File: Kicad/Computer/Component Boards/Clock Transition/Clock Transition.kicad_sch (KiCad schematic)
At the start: 14 parts, among them IC1 74LVC1G32GV,125, IC2 AP7365-33WG-7, IC3 74LVC1G02GV,125, IC4 74LVC74APW,118, IC5 74LVC08APW,112, IC7 74LVC74APW,118, J1 Conn_02x06_Counter_Clockwise

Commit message: Panelised Speed Board.
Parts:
- IC2: Garbage DiodesZetex AP7365-33WG-7, LDO Voltage Regulator, 600mA, 3.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 -> (none)
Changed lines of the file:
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@@
-			)
-		)
-		(property "Garbage" "DiodesZetex AP7365-33WG-7, LDO Voltage Regulator, 600mA, 3.3 V +/-2%, 2  6 Vin, 5-Pin SOT-25"
-			(at 130.81 186.182 0)
-			(effects
-				(font
-					(size 1.27 1.27)
-				)
-				(justify left)
-				(hide yes)
 			)
 		)

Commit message: Use VRML instead of STEPs for Graphics Board models.
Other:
- title: HCP65 W65C816 Clock Hold -> HCP65 Clock Transition
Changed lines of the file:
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@@
 	(paper "A4")
 	(title_block
-		(title "HCP65 W65C816 Clock Hold")
-		(date "2024-05-11")
-		(rev "V1")
+		(title "HCP65 Clock Transition")
+		(date "2025-01-04")
+		(rev "V0")
 	)
 	(junction

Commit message: Added Clock Transition.
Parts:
- added J2, J3: Pin_Header_01x06, SamacSys_Parts:PinHeader_1x06_P2.54mm_Vertical, symbol HCP65:Pin_Header_01x32
- IC5: Garbage NXP 74LVC08APW,112, Quad 2-Input AND Logic Gate, 1.2 3.6 V,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 -> (none)
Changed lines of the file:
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@@
-			)
-		)
-		(property "Garbage" "NXP 74LVC08APW,112, Quad 2-Input AND Logic Gate, 1.2  3.6 V, 14-Pin TSSOP"
-			(at 179.07 148.59 0)
-			(effects
-				(font
-					(size 1.27 1.27)
-				)
-				(hide yes)
 			)
 		)
@@
 			)
 		)
-		(property "Garbage" "NXP 74LVC08APW,112, Quad 2-Input AND Logic Gate, 1.2  3.6 V, 14-Pin TSSOP"
-			(at 90.17 93.98 0)
-			(effects
-				(font
-					(size 1.27 1.27)
-				)
-				(hide yes)
-			)
-		)
 		(pin "8"
 		)
@@
 	)
 	(symbol
+		(lib_id "HCP65:Pin_Header_01x32")
+		(at 53.34 135.89 0)
+		(unit 1)
+		(exclude_from_sim no)
+		(in_bom yes)
+		(on_board yes)
+		(dnp no)
+		(property "Reference" "J3"
+			(at 53.34 134.62 0)
+			(effects
+				(font
+					(size 1.27 1.27)
+				)
+			)
+		)
+		(property "Value" "Pin_Header_01x06"
+			(at 53.34 137.16 0)
+			(effects
+				(font
+					(size 1.27 1.27)
+				)
+			)
+		)
+		(property "Footprint" "SamacSys_Parts:PinHeader_1x06_P2.54mm_Vertical"
+			(at 53.34 139.7 0)
+			(effects
+				(font
+					(size 1.27 1.27)
+				)
+				(hide yes)
+			)
+		)
+		(property "Datasheet" "~"
+			(at 48.26 135.89 0)
+			(effects
+				(font
+					(size 1.27 1.27)
+				)
+				(hide yes)
+			)
+		)
+		(property "Description" ""
+			(at 53.34 135.89 0)
+			(effects
+				(font
+					(size 1.27 1.27)
+				)
+				(hide yes)
+			)
+		)
+		(instances
+			(project "Clock Transition"
+				(path "/5ce90b85-49a2-4937-86c7-662b0d6f8431"
+					(reference "J3")
+					(unit 1)
+				)
+			)
+		)
+	)
+	(symbol
 		(lib_id "Nexperia:74LVC08APW,112_Multi")
 		(at 209.55 90.17 0)
@@
 		(property "Silkscreen" "74LVC08"
 			(at 222.25 100.33 0)
-			(effects
-				(font
-					(size 1.27 1.27)
-				)
-				(hide yes)
-			)
-		)
-		(property "Garbage" "NXP 74LVC08APW,112, Quad 2-Input AND Logic Gate, 1.2  3.6 V, 14-Pin TSSOP"
-			(at 209.55 90.17 0)
 			(effects
 				(font
@@
 	)
 	(symbol
+		(lib_id "HCP65:Pin_Header_01x32")
+		(at 53.34 130.81 0)
+		(mirror y)
+		(unit 1)
+		(exclude_from_sim no)
+		(in_bom yes)
+		(on_board yes)
+		(dnp no)
+		(property "Reference" "J2"
+			(at 53.34 129.54 0)
+			(effects
+				(font
+					(size 1.27 1.27)
+				)
+			)
+		)
+		(property "Value" "Pin_Header_01x06"
+			(at 53.34 132.08 0)
+			(effects
+				(font
+					(size 1.27 1.27)
+				)
+			)
+		)
+		(property "Footprint" "SamacSys_Parts:PinHeader_1x06_P2.54mm_Vertical"
+			(at 53.34 134.62 0)
+			(effects
+				(font
+					(size 1.27 1.27)
+				)
+				(hide yes)
+			)
+		)
+		(property "Datasheet" "~"
+			(at 58.42 130.81 0)
+			(effects
+				(font
+					(size 1.27 1.27)
+				)
+				(hide yes)
+			)
+		)
+		(property "Description" ""
+			(at 53.34 130.81 0)
+			(effects
+				(font
+					(size 1.27 1.27)
+				)
+				(hide yes)
+			)
+		)
+		(instances
+			(project "Clock Transition"
+				(path "/5ce90b85-49a2-4937-86c7-662b0d6f8431"
+					(reference "J2")
+					(unit 1)
+				)
+			)
+		)
+	)
+	(symbol
 		(lib_id "HCP65:C_0805")
 		(at 107.95 175.26 0)
@@
 			(effects
 				(font
-					(size 1.27 1.27)
-				)
-				(hide yes)
-			)
-		)
-		(property "Garbage" "NXP 74LVC08APW,112, Quad 2-Input AND Logic Gate, 1.2  3.6 V, 14-Pin TSSOP"
-			(at 210.82 34.29 0)
-			(effects
-				(font

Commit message: Upgraded all Compnent Boards to Kicad 9.0.
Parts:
- renumbered C27 to C43, C27 to C44
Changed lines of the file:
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@@
 (kicad_sch
-	(version 20231120)
+	(version 20250114)
 	(generator "eeschema")
-	(generator_version "8.0")
+	(generator_version "9.0")
 	(paper "A4")
 	(title_block
@@
 	(label "GND"
 		(at 179.07 151.13 180)
-		(fields_autoplaced yes)
 		(effects
 			(font
@@
 	(label "3.3V"
 		(at 168.91 36.83 180)
-		(fields_autoplaced yes)
 		(effects
 			(font
@@
 	(label "3.3V"
 		(at 143.51 148.59 0)
-		(fields_autoplaced yes)
 		(effects
 			(font
@@
 	(label "GND"
 		(at 143.51 153.67 0)
-		(fields_autoplaced yes)
 		(effects
 			(font
@@
 	(label "3.3V"
 		(at 273.05 69.85 0)
-		(fields_autoplaced yes)
 		(effects
 			(font
@@
 	(label "Clock1_{Q}"
 		(at 194.31 36.83 0)
-		(fields_autoplaced yes)
 		(effects
 			(font
@@
 	(label "3.3V"
 		(at 115.57 92.71 0)
-		(fields_autoplaced yes)
 		(effects
 			(font
@@
 	(label "GND"
 		(at 168.91 44.45 180)
-		(fields_autoplaced yes)
 		(effects
 			(font
@@
 	(label "~{Reset}"
 		(at 129.54 97.79 180)
-		(fields_autoplaced yes)
 		(effects
 			(font
@@
 	(label "GND"
 		(at 91.44 43.18 180)
-		(fields_autoplaced yes)
 		(effects
 			(font
@@
 	(label "3.3V"
 		(at 123.19 184.15 180)
-		(fields_autoplaced yes)
 		(effects
 			(font
@@
 	(label "GND"
 		(at 113.03 175.26 0)
-		(fields_autoplaced yes)
 		(effects
 			(font
@@
 	(label "3.3V"
 		(at 123.19 175.26 180)
-		(fields_autoplaced yes)
 		(effects
 			(font
@@
 	(label "3.3V"
 		(at 92.71 175.26 180)
-		(fields_autoplaced yes)
 		(effects
 			(font
@@
 	(label "GND"
 		(at 90.17 99.06 180)
-		(fields_autoplaced yes)
 		(effects
 			(font
@@
 	(label "GND"
 		(at 210.82 39.37 180)
-		(fields_autoplaced yes)
 		(effects
 			(font
@@
 	(label "Clock"
 		(at 273.05 72.39 0)
-		(fields_autoplaced yes)
 		(effects
 			(font
@@
 	(label "3.3V"
 		(at 204.47 147.32 0)
-		(fields_autoplaced yes)
 		(effects
 			(font
@@
 	(label "GND"
 		(at 100.33 153.67 0)
-		(fields_autoplaced yes)
 		(effects
 			(font
@@
 	(label "~{Select Fast}"
 		(at 60.96 38.1 180)
-		(fields_autoplaced yes)
 		(effects
 			(font
@@
 	(label "3.3V"
 		(at 107.95 175.26 180)
-		(fields_autoplaced yes)
 		(effects
 			(font
@@
 	(label "GND"
 		(at 130.81 44.45 180)
-		(fields_autoplaced yes)
 		(effects
 			(font
@@
 	(label "GND"
 		(at 128.27 175.26 0)
-		(fields_autoplaced yes)
 		(effects
 			(font
@@
 	(label "3.3V"
 		(at 116.84 36.83 0)
-		(fields_autoplaced yes)
 		(effects
 			(font
@@
 	(label "GND"
 		(at 179.07 153.67 180)
-		(fields_autoplaced yes)
 		(effects
 			(font
@@
 	(label "3.3V"
 		(at 193.04 90.17 0)
-		(fields_autoplaced yes)
 		(effects
 			(font
@@
 	(label "3.3V"
 		(at 154.94 90.17 0)
-		(fields_autoplaced yes)
 		(effects
 			(font
@@
 	(label "Slow Clock"
 		(at 60.96 78.74 180)
-		(fields_autoplaced yes)
 		(effects
 			(font
@@
 	(label "3.3V"
 		(at 130.81 36.83 180)
-		(fields_autoplaced yes)
 		(effects
 			(font
@@
 	(label "GND"
 		(at 113.03 184.15 0)
-		(fields_autoplaced yes)
 		(effects
 			(font
@@
 	(label "Fast Clock"
 		(at 60.96 22.86 180)
-		(fields_autoplaced yes)
 		(effects
 			(font
@@
 	(label "3.3V"
 		(at 107.95 184.15 180)
-		(fields_autoplaced yes)
 		(effects
 			(font
@@
 	(label "GND"
 		(at 97.79 175.26 0)
-		(fields_autoplaced yes)
 		(effects
 			(font
@@
 	(label "GND"
 		(at 247.65 76.2 180)
-		(fields_autoplaced yes)
 		(effects
 			(font
@@
 	(label "~{Clock1}_{Q}"
 		(at 194.31 39.37 0)
-		(fields_autoplaced yes)
 		(effects
 			(font
@@
 	(label "GND"
 		(at 209.55 95.25 180)
-		(fields_autoplaced yes)
 		(effects
 			(font
@@
 	(label "GND"
 		(at 129.54 100.33 180)
-		(fields_autoplaced yes)
 		(effects
 			(font
@@
 	(label "Clock2_{Q}"
 		(at 193.04 92.71 0)
-		(fields_autoplaced yes)
 		(effects
 			(font
@@
 	(label "3.3V"
 		(at 167.64 92.71 180)
-		(fields_autoplaced yes)
 		(effects
 			(font
@@
 	(label "~{Reset}"
 		(at 130.81 41.91 180)
-		(fields_autoplaced yes)
 		(effects
 			(font
@@
 	(label "~{Reset}"
 		(at 167.64 97.79 180)
-		(fields_autoplaced yes)
 		(effects
 			(font
@@
 	(label "GND"
 		(at 167.64 100.33 180)
-		(fields_autoplaced yes)
 		(effects
 			(font
@@
 	(label "GND"
 		(at 179.07 148.59 180)
-		(fields_autoplaced yes)
 		(effects
 			(font
@@
 	(label "3.3V"
 		(at 194.31 34.29 0)
-		(fields_autoplaced yes)
 		(effects
 			(font
@@
 	(label "GND"
 		(at 128.27 184.15 0)
-		(fields_autoplaced yes)
 		(effects
 			(font
@@
 	(label "5V"
 		(at 93.98 148.59 180)
-		(fields_autoplaced yes)
 		(effects
 			(font
@@
 	(label "3.3V"
 		(at 236.22 33.02 0)
-		(fields_autoplaced yes)
 		(effects
 			(font
@@
 	(label "3.3V"
 		(at 156.21 34.29 0)
-		(fields_autoplaced yes)
 		(effects
 			(font
@@
 	(label "3.3V"
 		(at 129.54 92.71 180)
-		(fields_autoplaced yes)
 		(effects
 			(font
@@
 	(label "~{Reset}"
 		(at 168.91 41.91 180)
-		(fields_autoplaced yes)
 		(effects
 			(font
@@
 	(label "GND"
 		(at 109.22 153.67 180)
-		(fields_autoplaced yes)
 		(effects
 			(font
@@
 	(label "3.3V"
 		(at 234.95 88.9 0)
-		(fields_autoplaced yes)
 		(effects
 			(font
@@
 		(on_board yes)
 		(dnp no)
-		(property "Reference" "C27"
+		(property "Reference" "C44"
 			(at 140.716 151.13 0)
 			(effects
@@
 		(on_board yes)
 		(dnp no)
-		(property "Reference" "C27"
+		(property "Reference" "C43"
 			(at 97.536 151.13 0)
 			(effects
@@
 		)
 	)
+	(embedded_fonts no)
 )

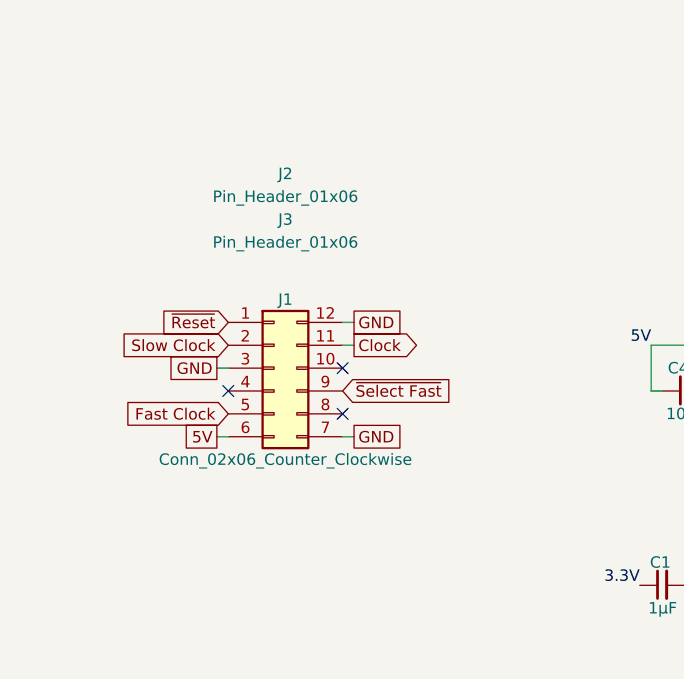
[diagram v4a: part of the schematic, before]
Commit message: Changing component board sockets.
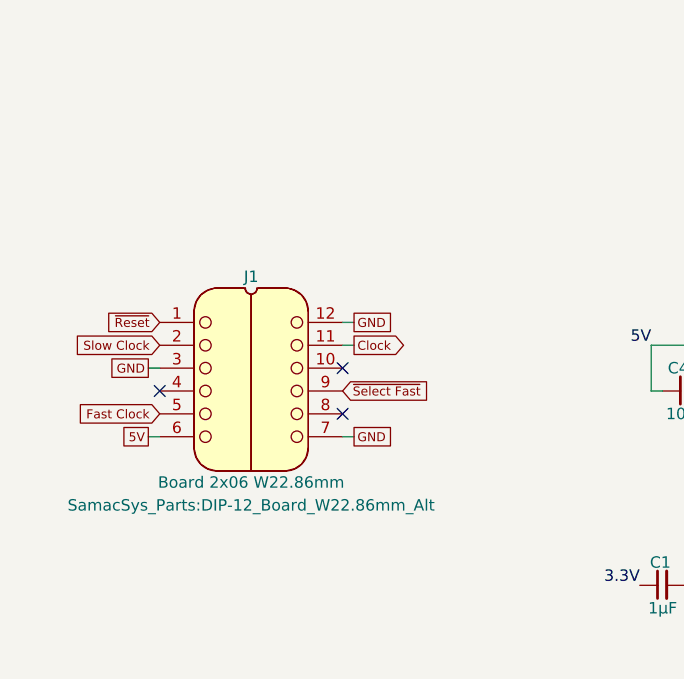
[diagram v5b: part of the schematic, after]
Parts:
- removed J2, J3: Pin_Header_01x06, SamacSys_Parts:PinHeader_1x06_P2.54mm_Vertical, symbol HCP65:Pin_Header_01x32
- IC3: Garbage 74LVC1G02 - Single 2-input NOR gate@en-us -> (none)
- J1: value Conn_02x06_Counter_Clockwise -> Board 2x06 W22.86mm; symbol Connector_Generic:Conn_02x06_Counter_Clockwise -> HCP65:Board_02x06_W22.86mm
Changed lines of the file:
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@@
 	)
 	(no_connect
-		(at 46.99 153.67)
+		(at 39.37 153.67)
 	)
 	(no_connect
@@
 	(wire
 		(pts
-			(xy 45.72 151.13) (xy 46.99 151.13)
+			(xy 38.1 151.13) (xy 39.37 151.13)
 		)
 		(stroke
@@
 	(wire
 		(pts
-			(xy 45.72 158.75) (xy 46.99 158.75)
+			(xy 38.1 158.75) (xy 39.37 158.75)
 		)
 		(stroke
@@
 		(effects
 			(font
-				(size 1.27 1.27)
+				(size 1 1)
 			)
 			(justify left)
@@
 	(global_label "5V"
 		(shape passive)
-		(at 45.72 158.75 180)
+		(at 38.1 158.75 180)
 		(fields_autoplaced yes)
 		(effects
 			(font
-				(size 1.27 1.27)
+				(size 1 1)
 			)
 			(justify right)
 		)
 		(property "Intersheetrefs" "${INTERSHEET_REFS}"
-			(at 41.6274 158.75 0)
+			(at 34.0074 158.75 0)
 			(effects
 				(font
@@
 		(effects
 			(font
-				(size 1.27 1.27)
+				(size 1 1)
 			)
 			(justify left)
@@
 		(effects
 			(font
-				(size 1.27 1.27)
+				(size 1 1)
 			)
 			(justify left)
@@
 		(effects
 			(font
-				(size 1.27 1.27)
+				(size 1 1)
 			)
 			(justify left)
@@
 	(global_label "Fast Clock"
 		(shape input)
-		(at 46.99 156.21 180)
+		(at 39.37 156.21 180)
 		(fields_autoplaced yes)
 		(effects
 			(font
-				(size 1.27 1.27)
+				(size 1 1)
 			)
 			(justify right)
 		)
 		(property "Intersheetrefs" "${INTERSHEET_REFS}"
-			(at 33.8449 156.21 0)
+			(at 26.2249 156.21 0)
 			(effects
 				(font
@@
 	(global_label "~{Reset}"
 		(shape input)
-		(at 46.99 146.05 180)
+		(at 39.37 146.05 180)
 		(fields_autoplaced yes)
 		(effects
 			(font
-				(size 1.27 1.27)
+				(size 1 1)
 			)
 			(justify right)
 		)
 		(property "Intersheetrefs" "${INTERSHEET_REFS}"
-			(at 38.8038 146.05 0)
+			(at 31.1838 146.05 0)
 			(effects
 				(font
@@
 	(global_label "GND"
 		(shape passive)
-		(at 45.72 151.13 180)
+		(at 38.1 151.13 180)
 		(fields_autoplaced yes)
 		(effects
 			(font
-				(size 1.27 1.27)
+				(size 1 1)
 			)
 			(justify right)
 		)
 		(property "Intersheetrefs" "${INTERSHEET_REFS}"
-			(at 40.055 151.13 0)
+			(at 32.435 151.13 0)
 			(effects
 				(font
@@
 	(global_label "Slow Clock"
 		(shape input)
-		(at 46.99 148.59 180)
+		(at 39.37 148.59 180)
 		(fields_autoplaced yes)
 		(effects
 			(font
-				(size 1.27 1.27)
+				(size 1 1)
 			)
 			(justify right)
 		)
 		(property "Intersheetrefs" "${INTERSHEET_REFS}"
-			(at 33.4821 148.59 0)
+			(at 25.8621 148.59 0)
 			(effects
 				(font
@@
 	)
 	(symbol
-		(lib_id "Connector_Generic:Conn_02x06_Counter_Clockwise")
-		(at 52.07 151.13 0)
+		(lib_id "HCP65:Board_02x06_W22.86mm")
+		(at 49.53 146.05 0)
 		(unit 1)
 		(exclude_from_sim no)
@@
 		(dnp no)
 		(property "Reference" "J1"
-			(at 53.34 143.51 0)
+			(at 49.53 140.97 0)
 			(effects
 				(font
@@
 			)
 		)
-		(property "Value" "Conn_02x06_Counter_Clockwise"
-			(at 53.34 161.29 0)
+		(property "Value" "Board 2x06 W22.86mm"
+			(at 49.53 163.83 0)
 			(effects
 				(font
@@
 		)
 		(property "Footprint" "SamacSys_Parts:DIP-12_Board_W22.86mm_Alt"
-			(at 52.07 151.13 0)
+			(at 49.53 166.37 0)
 			(effects
 				(font
 					(size 1.27 1.27)
 				)
-				(hide yes)
 			)
 		)
-		(property "Datasheet" "~"
-			(at 52.07 151.13 0)
+		(property "Datasheet" ""
+			(at 49.53 191.77 0)
 			(effects
 				(font
@@
 			)
 		)
-		(property "Description" "Generic connector, double row, 02x06, counter clockwise pin numbering scheme (similar to DIP package numbering), script generated (kicad-library-utils/schlib/autogen/connector/)"
-			(at 52.07 151.13 0)
+		(property "Description" ""
+			(at 49.53 163.83 0)
 			(effects
 				(font
@@
 			)
 		)
-		(property "Garbage" "74LVC1G02 - Single 2-input NOR gate@en-us"
-			(at 91.44 38.1 0)
-			(effects
-				(font
-					(size 1.27 1.27)
-				)
-				(hide yes)
-			)
-		)
 		(pin "1"
 		)
@@
 	)
 	(symbol
-		(lib_id "HCP65:Pin_Header_01x32")
-		(at 53.34 135.89 0)
-		(unit 1)
-		(exclude_from_sim no)
-		(in_bom yes)
-		(on_board yes)
-		(dnp no)
-		(property "Reference" "J3"
-			(at 53.34 134.62 0)
-			(effects
-				(font
-					(size 1.27 1.27)
-				)
-			)
-		)
-		(property "Value" "Pin_Header_01x06"
-			(at 53.34 137.16 0)
-			(effects
-				(font
-					(size 1.27 1.27)
-				)
-			)
-		)
-		(property "Footprint" "SamacSys_Parts:PinHeader_1x06_P2.54mm_Vertical"
-			(at 53.34 139.7 0)
-			(effects
-				(font
-					(size 1.27 1.27)
-				)
-				(hide yes)
-			)
-		)
-		(property "Datasheet" "~"
-			(at 48.26 135.89 0)
-			(effects
-				(font
-					(size 1.27 1.27)
-				)
-				(hide yes)
-			)
-		)
-		(property "Description" ""
-			(at 53.34 135.89 0)
-			(effects
-				(font
-					(size 1.27 1.27)
-				)
-				(hide yes)
-			)
-		)
-		(instances
-			(project "Clock Transition"
-				(path "/5ce90b85-49a2-4937-86c7-662b0d6f8431"
-					(reference "J3")
-					(unit 1)
-				)
-			)
-		)
-	)
-	(symbol
 		(lib_id "Nexperia:74LVC08APW,112_Multi")
 		(at 209.55 90.17 0)
@@
 					(unit 1)
 				)
-			)
-		)
-	)
-	(symbol
-		(lib_id "HCP65:Pin_Header_01x32")
-		(at 53.34 130.81 0)
-		(mirror y)
-		(unit 1)
-		(exclude_from_sim no)
-		(in_bom yes)
-		(on_board yes)
-		(dnp no)
-		(property "Reference" "J2"
-			(at 53.34 129.54 0)
-			(effects
-				(font
-					(size 1.27 1.27)
-				)
-			)
-		)
-		(property "Value" "Pin_Header_01x06"
-			(at 53.34 132.08 0)
-			(effects
-				(font
-					(size 1.27 1.27)
-				)
-			)
-		)
-		(property "Footprint" "SamacSys_Parts:PinHeader_1x06_P2.54mm_Vertical"
-			(at 53.34 134.62 0)
-			(effects
-				(font
-					(size 1.27 1.27)
-				)
-				(hide yes)
-			)
-		)
-		(property "Datasheet" "~"
-			(at 58.42 130.81 0)
-			(effects
-				(font
-					(size 1.27 1.27)
-				)
-				(hide yes)
-			)
-		)
-		(property "Description" ""
-			(at 53.34 130.81 0)
-			(effects
-				(font
-					(size 1.27 1.27)
-				)
-				(hide yes)
-			)
-		)
-		(instances
-			(project "Clock Transition"
-				(path "/5ce90b85-49a2-4937-86c7-662b0d6f8431"
-					(reference "J2")
-					(unit 1)
-				)
